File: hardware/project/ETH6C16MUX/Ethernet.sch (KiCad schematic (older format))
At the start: 38 parts

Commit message: Schematic design
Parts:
- L?: symbol ETH6C12MUX:749010012A -> ETH6C16MUX:749010012A
- U?: symbol ETH6C12MUX:LAN8742 -> ETH6C16MUX:LAN8742
- U? (x2): symbol ETH6C12MUX:LC03-3.3 -> ETH6C16MUX:LC03-3.3
- U? (x2): symbol ETH6C12MUX:SR3.3 -> ETH6C16MUX:SR3.3
- U?: symbol ETH6C12MUX:ASDM -> ETH6C16MUX:ASDM
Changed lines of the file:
@@
 EESchema Schematic File Version 4
-LIBS:ETH6C12MUX-cache
+LIBS:ETH6C16MUX-cache
 EELAYER 30 0
 EELAYER END
@@
 $EndDescr
 $Comp
-L ETH6C12MUX:LAN8742 U?
+L ETH6C16MUX:LAN8742 U?
 U 1 1 5D7788FE
 P 3100 3400
@@
 $EndComp
 $Comp
-L ETH6C12MUX:749010012A L?
+L ETH6C16MUX:749010012A L?
 U 1 1 5D78EEFA
 P 7950 3200
@@
 	3000 1750 3000 2200
 $Comp
-L ETH6C12MUX:LC03-3.3 U?
+L ETH6C16MUX:LC03-3.3 U?
 U 1 1 5D7B5D01
 P 10050 2850
@@
 $EndComp
 $Comp
-L ETH6C12MUX:LC03-3.3 U?
+L ETH6C16MUX:LC03-3.3 U?
 U 1 1 5D7B67F8
 P 10050 3650
@@
 	6500 3200 7100 3200
 $Comp
-L ETH6C12MUX:+3.3V_MCU #PWR?
+L ETH6C16MUX:+3.3V_MCU #PWR?
 U 1 1 5D9535B8
 P 1800 1000
@@
 Connection ~ 1800 1050
 $Comp
-L ETH6C12MUX:+3.3V_MCU #PWR?
+L ETH6C16MUX:+3.3V_MCU #PWR?
 U 1 1 5D95A1B1
 P 3100 5100
@@
 	2300 4100 1250 4100
 $Comp
-L ETH6C12MUX:SR3.3 U?
+L ETH6C16MUX:SR3.3 U?
 U 1 1 5D9B1A51
 P 6000 4600
@@
 $EndComp
 $Comp
-L ETH6C12MUX:SR3.3 U?
+L ETH6C16MUX:SR3.3 U?
 U 1 1 5D9B4299
 P 6000 3800
@@
 ETH_REFCLK_PHY_50MHZ
 $Comp
-L ETH6C12MUX:ASDM U?
+L ETH6C16MUX:ASDM U?
 U 1 1 5DB00494
 P 5100 5900
@@
 $EndComp
 $Comp
-L ETH6C12MUX:+3.3V_MCU #PWR?
+L ETH6C16MUX:+3.3V_MCU #PWR?
 U 1 1 5DB22922
 P 5100 5450
@@
 	5100 5500 5100 5450
 $Comp
-L ETH6C12MUX:+3.3V_MCU #PWR?
+L ETH6C16MUX:+3.3V_MCU #PWR?
 U 1 1 5DB320BA
 P 5100 6800

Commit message: FPGA schematic
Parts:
- removed U?: ASDM1-50.000MHZ-LC-T, symbol ETH6C16MUX:ASDM
- added U?: ASDM1-50.000MHZ-LC-T, Oscillator:Oscillator_SMD_Abracon_ASDMB-4Pin_2.5x2.0mm, symbol Oscillator:ASDMB-xxxMHz
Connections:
- net labels added: GND
- net labels removed: GNDD
- wire segments 160 -> 163
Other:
- moved on the sheet: C?, R?

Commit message: Schematic design
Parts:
- removed C? (x2): 100p, symbol Device:C
- added R211, R215: 220, symbol Device:R
- C201, C202, C204, C205, C206, C207, C210, C213: renamed from C?; footprint (none) -> ETH6C16MXU:C_0603_A_Pad1.05x0.95mm_HandSolder
- D201, D202: renamed from D?; footprint (none) -> LED_SMD:LED_0603_1608Metric_Pad1.05x0.95mm_HandSolder
- L201: renamed from L?; footprint (none) -> ETH6C16MXU:749010012A
- R201, R202, R203, R204, R206, R207: renamed from R?; footprint (none) -> Resistor_SMD:R_0603_1608Metric_Pad1.05x0.95mm_HandSolder
- gave numbers to parts that had none: 19
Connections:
- net labels added: +3.3V
- net labels removed: +3.3V_MCU

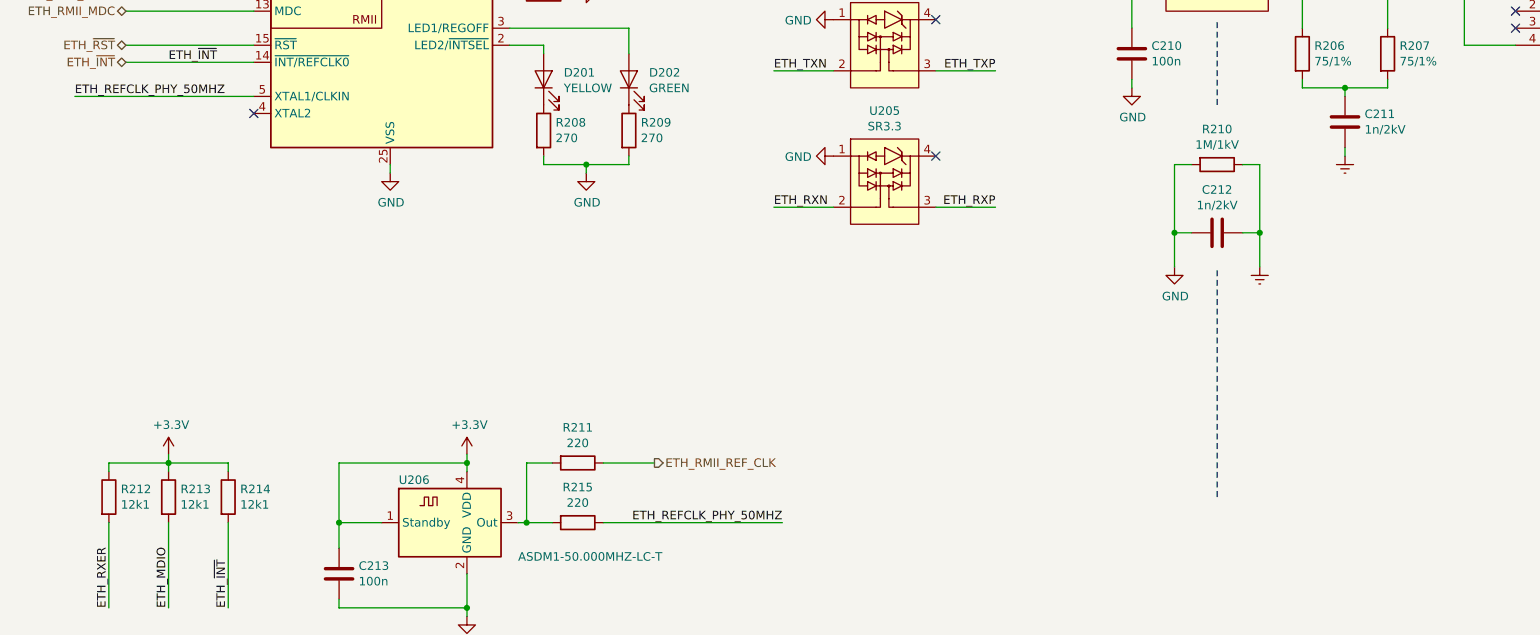
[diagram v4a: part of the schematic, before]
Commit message: PCB design, need to redesign of the board to board connectors.
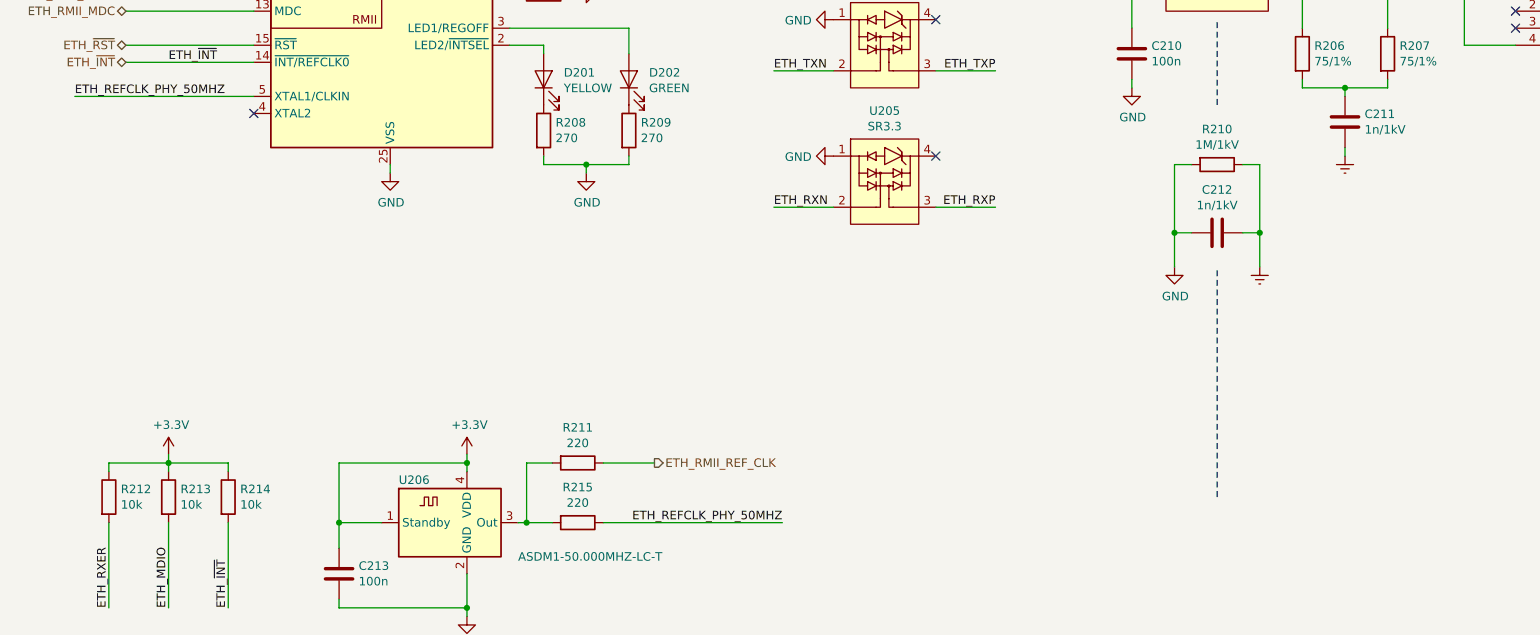
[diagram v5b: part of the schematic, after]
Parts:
- C203, C209: footprint (none) -> ETH6C16MXU:C_0603_B_Pad1.05x0.95mm_HandSolder
- C208: footprint (none) -> Capacitor_SMD:C_0603_1608Metric_Pad1.05x0.95mm_HandSolder
- C211, C212: value 1n/2kV -> 1n/1kV; footprint (none) -> Capacitor_SMD:C_1206_3216Metric_Pad1.42x1.75mm_HandSolder
- FB201: footprint (none) -> ETH6C16MXU:R_0805_D_Pad1.15x1.40mm_HandSolder
- R205, R211, R215: footprint (none) -> Resistor_SMD:R_0603_1608Metric_Pad1.05x0.95mm_HandSolder
- R208, R209: footprint (none) -> ETH6C16MXU:R_0603_E_Pad1.05x0.95mm_HandSolder
- R210: footprint (none) -> Resistor_SMD:R_1206_3216Metric_Pad1.42x1.75mm_HandSolder
- R212, R213, R214: value 12k1 -> 10k; footprint (none) -> ETH6C16MXU:R_0603_E_Pad1.05x0.95mm_HandSolder
- U201, U203: footprint (none) -> ETH6C16MXU:SO8E
- U204, U205: footprint (none) -> Package_TO_SOT_SMD:SOT-143_Handsoldering
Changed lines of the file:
@@
 F 0 "R205" V 3900 3500 50  0000 C CNN
 F 1 "12k1" V 4000 3500 50  0000 C CNN
-F 2 "" V 3930 3500 50  0001 C CNN
+F 2 "Resistor_SMD:R_0603_1608Metric_Pad1.05x0.95mm_HandSolder" V 3930 3500 50  0001 C CNN
 F 3 "~" H 4000 3500 50  0001 C CNN
 	1    4000 3500
@@
 F 0 "R208" H 4070 4346 50  0000 L CNN
 F 1 "270" H 4070 4255 50  0000 L CNN
-F 2 "" V 3930 4300 50  0001 C CNN
+F 2 "ETH6C16MXU:R_0603_E_Pad1.05x0.95mm_HandSolder" V 3930 4300 50  0001 C CNN
 F 3 "~" H 4000 4300 50  0001 C CNN
 	1    4000 4300
@@
 F 0 "R209" H 4570 4346 50  0000 L CNN
 F 1 "270" H 4570 4255 50  0000 L CNN
-F 2 "" V 4430 4300 50  0001 C CNN
+F 2 "ETH6C16MXU:R_0603_E_Pad1.05x0.95mm_HandSolder" V 4430 4300 50  0001 C CNN
 F 3 "~" H 4500 4300 50  0001 C CNN
 	1    4500 4300
@@
 F 0 "C208" H 1915 1996 50  0000 L CNN
 F 1 "470p" H 1915 1905 50  0000 L CNN
-F 2 "" H 1838 1800 50  0001 C CNN
+F 2 "Capacitor_SMD:C_0603_1608Metric_Pad1.05x0.95mm_HandSolder" H 1838 1800 50  0001 C CNN
 F 3 "~" H 1800 1950 50  0001 C CNN
 	1    1800 1950
@@
 F 0 "C209" H 2365 1996 50  0000 L CNN
 F 1 "1u" H 2365 1905 50  0000 L CNN
-F 2 "" H 2288 1800 50  0001 C CNN
+F 2 "ETH6C16MXU:C_0603_B_Pad1.05x0.95mm_HandSolder" H 2288 1800 50  0001 C CNN
 F 3 "~" H 2250 1950 50  0001 C CNN
 	1    2250 1950
@@
 P 8700 4250
 F 0 "C211" H 8815 4296 50  0000 L CNN
-F 1 "1n/2kV" H 8815 4205 50  0000 L CNN
-F 2 "" H 8738 4100 50  0001 C CNN
+F 1 "1n/1kV" H 8815 4205 50  0000 L CNN
+F 2 "Capacitor_SMD:C_1206_3216Metric_Pad1.42x1.75mm_HandSolder" H 8738 4100 50  0001 C CNN
 F 3 "~" H 8700 4250 50  0001 C CNN
 	1    8700 4250
@@
 F 0 "R210" V 7743 4500 50  0000 C CNN
 F 1 "1M/1kV" V 7834 4500 50  0000 C CNN
-F 2 "" V 7880 4500 50  0001 C CNN
+F 2 "Resistor_SMD:R_1206_3216Metric_Pad1.42x1.75mm_HandSolder" V 7880 4500 50  0001 C CNN
 F 3 "~" H 7950 4500 50  0001 C CNN
 	1    7950 4500
@@
 P 7950 4900
 F 0 "C212" V 7698 4900 50  0000 C CNN
-F 1 "1n/2kV" V 7789 4900 50  0000 C CNN
-F 2 "" H 7988 4750 50  0001 C CNN
+F 1 "1n/1kV" V 7789 4900 50  0000 C CNN
+F 2 "Capacitor_SMD:C_1206_3216Metric_Pad1.42x1.75mm_HandSolder" H 7988 4750 50  0001 C CNN
 F 3 "~" H 7950 4900 50  0001 C CNN
 	1    7950 4900
@@
 F 0 "U201" H 10050 3287 60  0000 C CNN
 F 1 "LC03-3.3" H 10050 3181 60  0000 C CNN
-F 2 "" H 10050 2850 60  0001 C CNN
+F 2 "ETH6C16MXU:SO8E" H 10050 2850 60  0001 C CNN
 F 3 "" H 10050 2850 60  0000 C CNN
 	1    10050 2850
@@
 F 0 "U203" H 10050 4087 60  0000 C CNN
 F 1 "LC03-3.3" H 10050 3981 60  0000 C CNN
-F 2 "" H 10050 3650 60  0001 C CNN
+F 2 "ETH6C16MXU:SO8E" H 10050 3650 60  0001 C CNN
 F 3 "" H 10050 3650 60  0000 C CNN
 	1    10050 3650
@@
 F 0 "FB201" V 2826 1050 50  0000 C CNN
 F 1 "742792031" V 2917 1050 50  0000 C CNN
-F 2 "" V 3030 1050 50  0001 C CNN
+F 2 "ETH6C16MXU:R_0805_D_Pad1.15x1.40mm_HandSolder" V 3030 1050 50  0001 C CNN
 F 3 "~" H 3100 1050 50  0001 C CNN
 	1    3100 1050
@@
 F 0 "C203" H 3465 1296 50  0000 L CNN
 F 1 "1u" H 3465 1205 50  0000 L CNN
-F 2 "" H 3388 1100 50  0001 C CNN
+F 2 "ETH6C16MXU:C_0603_B_Pad1.05x0.95mm_HandSolder" H 3388 1100 50  0001 C CNN
 F 3 "~" H 3350 1250 50  0001 C CNN
 	1    3350 1250
@@
 P 1450 6450
 F 0 "R212" H 1520 6496 50  0000 L CNN
-F 1 "12k1" H 1520 6405 50  0000 L CNN
-F 2 "" V 1380 6450 50  0001 C CNN
+F 1 "10k" H 1520 6405 50  0000 L CNN
+F 2 "ETH6C16MXU:R_0603_E_Pad1.05x0.95mm_HandSolder" V 1380 6450 50  0001 C CNN
 F 3 "~" H 1450 6450 50  0001 C CNN
 	1    1450 6450
@@
 P 1800 6450
 F 0 "R213" H 1870 6496 50  0000 L CNN
-F 1 "12k1" H 1870 6405 50  0000 L CNN
-F 2 "" V 1730 6450 50  0001 C CNN
+F 1 "10k" H 1870 6405 50  0000 L CNN
+F 2 "ETH6C16MXU:R_0603_E_Pad1.05x0.95mm_HandSolder" V 1730 6450 50  0001 C CNN
 F 3 "~" H 1800 6450 50  0001 C CNN
 	1    1800 6450
@@
 P 2150 6450
 F 0 "R214" H 2220 6496 50  0000 L CNN
-F 1 "12k1" H 2220 6405 50  0000 L CNN
-F 2 "" V 2080 6450 50  0001 C CNN
+F 1 "10k" H 2220 6405 50  0000 L CNN
+F 2 "ETH6C16MXU:R_0603_E_Pad1.05x0.95mm_HandSolder" V 2080 6450 50  0001 C CNN
 F 3 "~" H 2150 6450 50  0001 C CNN
 	1    2150 6450
@@
 F 0 "U205" H 6000 5015 50  0000 C CNN
 F 1 "SR3.3" H 6000 4924 50  0000 C CNN
-F 2 "" H 6125 4800 50  0001 C CNN
+F 2 "Package_TO_SOT_SMD:SOT-143_Handsoldering" H 6125 4800 50  0001 C CNN
 F 3 "" H 6125 4800 50  0001 C CNN
 	1    6000 4600
@@
 F 0 "U204" H 6000 4215 50  0000 C CNN
 F 1 "SR3.3" H 6000 4124 50  0000 C CNN
-F 2 "" H 6125 4000 50  0001 C CNN
+F 2 "Package_TO_SOT_SMD:SOT-143_Handsoldering" H 6125 4000 50  0001 C CNN
 F 3 "" H 6125 4000 50  0001 C CNN
 	1    6000 3800
@@
 F 0 "R211" V 3993 6250 50  0000 C CNN
 F 1 "220" V 4084 6250 50  0000 C CNN
-F 2 "" V 4130 6250 50  0001 C CNN
+F 2 "Resistor_SMD:R_0603_1608Metric_Pad1.05x0.95mm_HandSolder" V 4130 6250 50  0001 C CNN
 F 3 "~" H 4200 6250 50  0001 C CNN
 	1    4200 6250
@@
 F 0 "R215" V 3993 6600 50  0000 C CNN
 F 1 "220" V 4084 6600 50  0000 C CNN
-F 2 "" V 4130 6600 50  0001 C CNN
+F 2 "Resistor_SMD:R_0603_1608Metric_Pad1.05x0.95mm_HandSolder" V 4130 6600 50  0001 C CNN
 F 3 "~" H 4200 6600 50  0001 C CNN
 	1    4200 6600

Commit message: PCB layout, deleted USB.
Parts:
- U202: footprint Package_DFN_QFN:QFN-24-1EP_4x4mm_P0.5mm_EP2.6x2.6mm -> Package_DFN_QFN:QFN-24-1EP_4x4mm_P0.5mm_EP2.6x2.6mm_ThermalVias
- U204, U205: footprint Package_TO_SOT_SMD:SOT-143_Handsoldering -> Package_TO_SOT_SMD:SOT-143
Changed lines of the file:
@@
 $Descr A4 11693 8268
 encoding utf-8
-Sheet 2 8
+Sheet 2 7
 Title "Ethernet"
 Date ""
@@
 F 0 "U202" H 2450 4550 50  0000 C CNN
 F 1 "LAN8742" H 3550 4550 50  0000 C CNN
-F 2 "Package_DFN_QFN:QFN-24-1EP_4x4mm_P0.5mm_EP2.6x2.6mm" H 3150 2350 50  0001 L CNN
+F 2 "Package_DFN_QFN:QFN-24-1EP_4x4mm_P0.5mm_EP2.6x2.6mm_ThermalVias" H 3150 2350 50  0001 L CNN
 F 3 "http://ww1.microchip.com/downloads/en/DeviceDoc/8720a.pdf" H 2900 2450 50  0001 C CNN
 	1    3100 3400
@@
 F 0 "U205" H 6000 5015 50  0000 C CNN
 F 1 "SR3.3" H 6000 4924 50  0000 C CNN
-F 2 "Package_TO_SOT_SMD:SOT-143_Handsoldering" H 6125 4800 50  0001 C CNN
+F 2 "Package_TO_SOT_SMD:SOT-143" H 6125 4800 50  0001 C CNN
 F 3 "" H 6125 4800 50  0001 C CNN
 	1    6000 4600
@@
 F 0 "U204" H 6000 4215 50  0000 C CNN
 F 1 "SR3.3" H 6000 4124 50  0000 C CNN
-F 2 "Package_TO_SOT_SMD:SOT-143_Handsoldering" H 6125 4000 50  0001 C CNN
+F 2 "Package_TO_SOT_SMD:SOT-143" H 6125 4000 50  0001 C CNN
 F 3 "" H 6125 4000 50  0001 C CNN
 	1    6000 3800
